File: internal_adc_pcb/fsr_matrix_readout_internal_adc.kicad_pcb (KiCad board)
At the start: 2 copper layers, 50 x 65 mm, 97 parts, among them J1 Conn_01x22, J2 Conn_01x22, U1 RS2323XUTQK10, U10 TLV9061xDBV, U11 SN74AHC138RGYR, U12 SN74AHC138RGYR, U13 SN74LVC1G14DCKR_C19829630, U14 TLV9064, U15 TLV9064, U16 TLV9064, U17 TLV9064, U2 RS2323XUTQK10, U3 RS2323XUTQK10, U4 RS2323XUTQK10, U5 RS2323XUTQK10, U6 RS2323XUTQK10, U7 RS2323XUTQK10, U8 RS2323XUTQK10, U9 TPS7A2033PDBVR

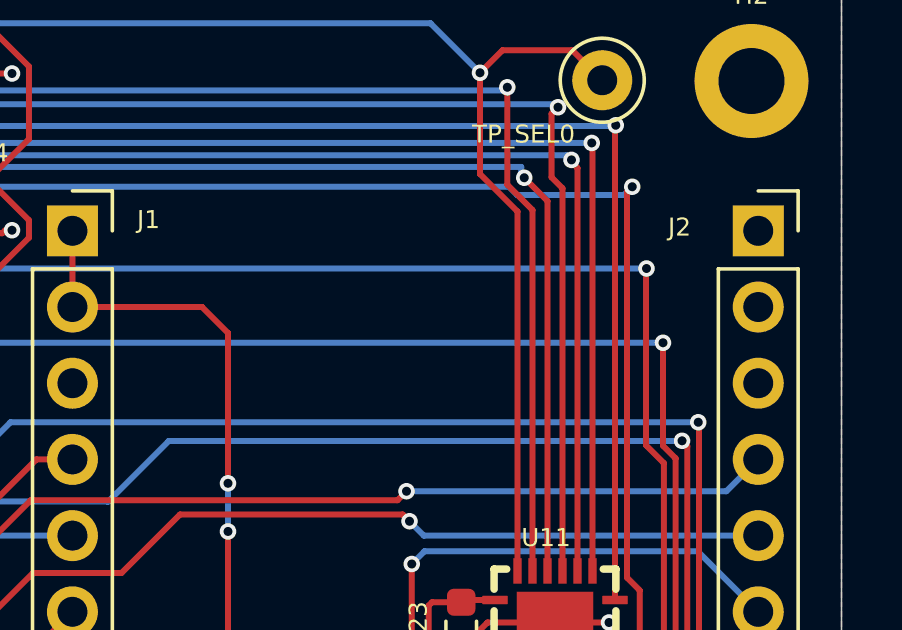
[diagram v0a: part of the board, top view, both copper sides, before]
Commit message: add fab files; add silkscreen for ver and author
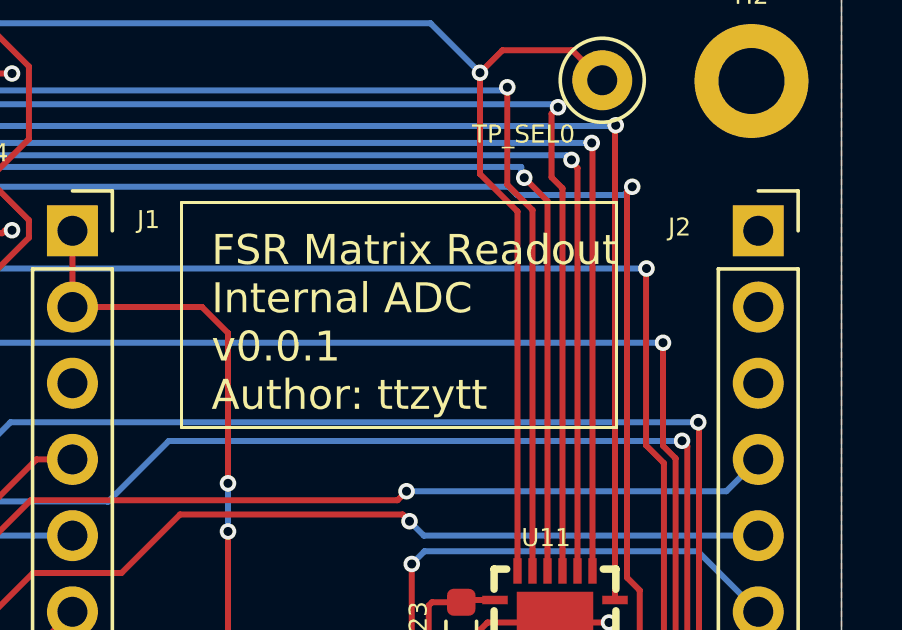
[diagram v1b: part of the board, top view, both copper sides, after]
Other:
- board text added: "FSR Matrix Readout Internal ADC v0.0.1 Author: ttzytt"
